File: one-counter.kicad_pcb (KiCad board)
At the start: 2 copper layers, 15 parts, among them J1 Conn_01x07-L, J2 Conn_01x07-R, U1 L7805, U2 555-L, U3 555-R, U4 74LS90-L, U5 74LS90-R, U6 7447-L, U7 7447-R, U8 5082-7650-L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

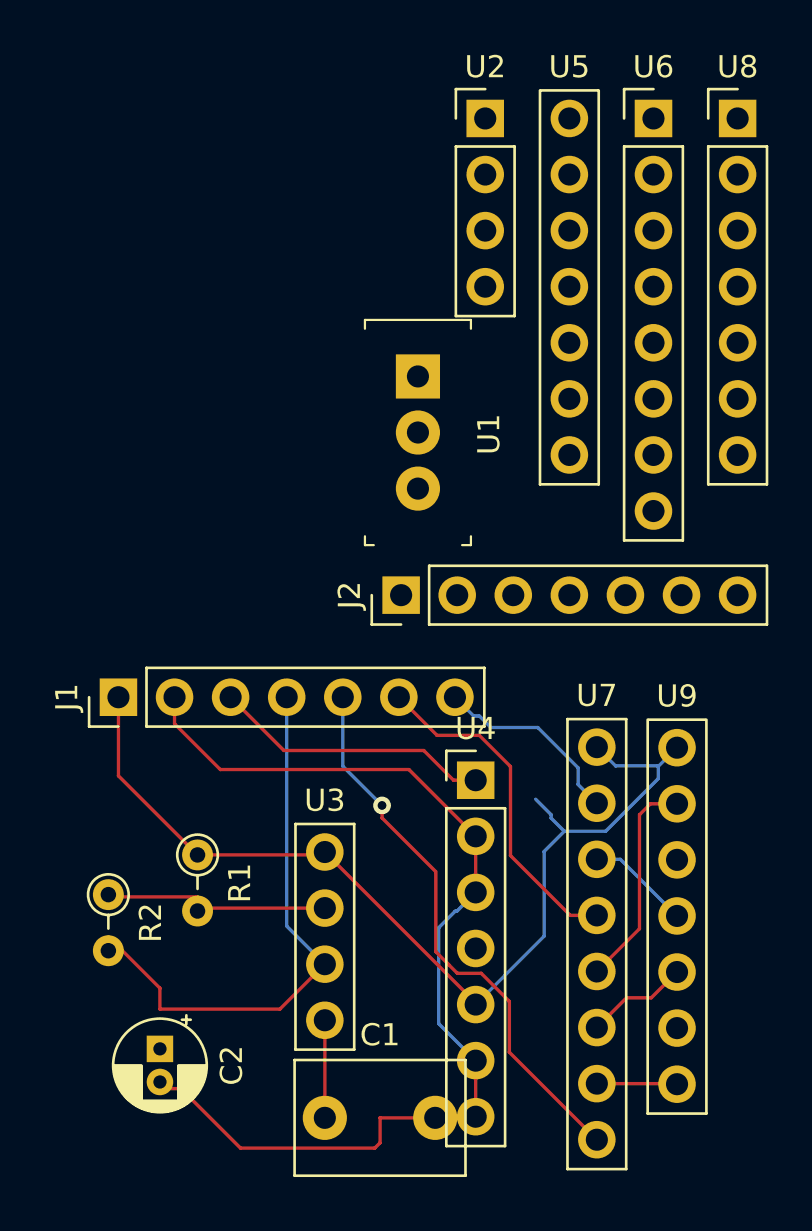
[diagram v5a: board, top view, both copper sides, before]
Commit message: bottom footprints mostly in place
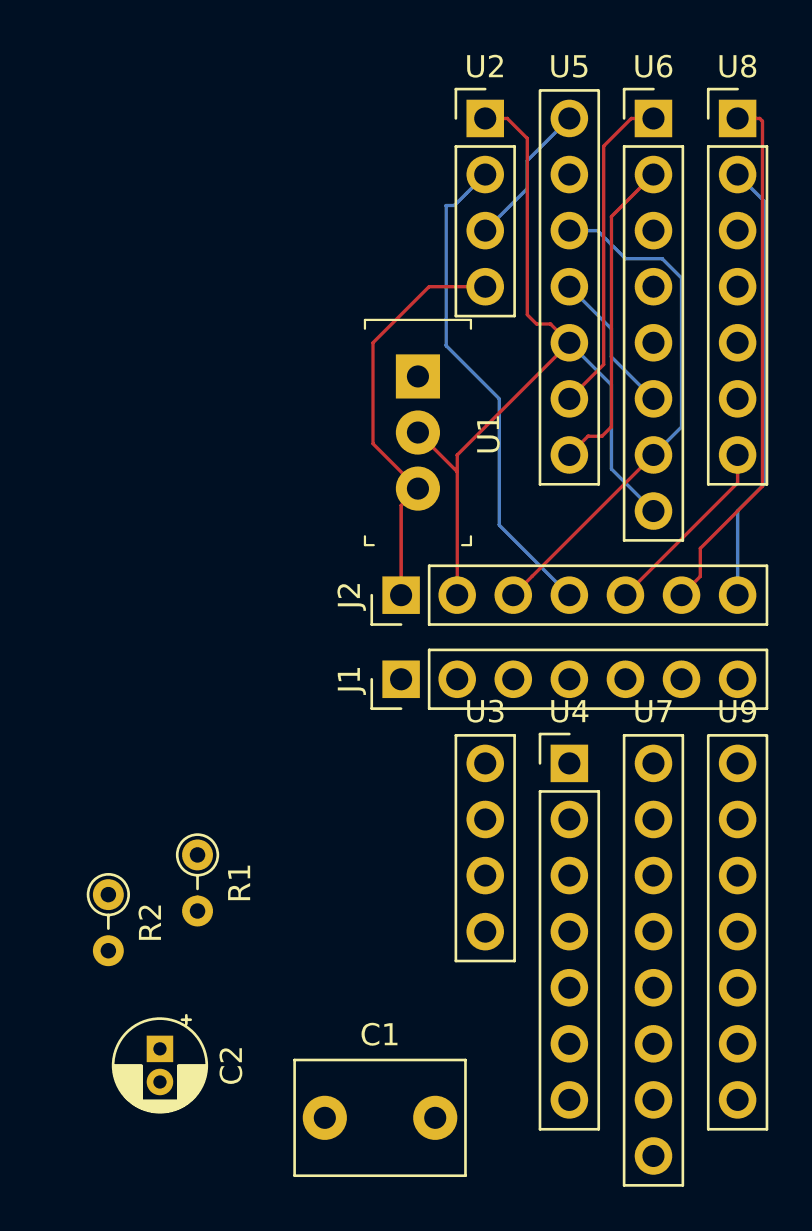
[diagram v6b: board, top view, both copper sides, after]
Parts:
- moved J1 12.8 mm to (162.6, 114.3)
- moved U3 8.30 mm to (166.4, 118.1)
- moved U4 4.31 mm to (170.2, 118.1)
- moved U9 2.83 mm to (177.8, 118.1)
- moved U7 2.67 mm to (174.0, 118.1)
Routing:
- net +5V: track 45.8 -> 18.7 mm
- net U7-9: track 25.5 -> 0.00 mm, vias 1 -> 0
- net U3-6: track 25.4 -> 0.00 mm
- net U8-1: track 0.00 -> 24.2 mm
- net U5-12: track 0.00 -> 23.5 mm
- net U2-2: track 0.00 -> 22.3 mm
- net U8-2: track 0.00 -> 20.1 mm
- net U7-13: track 15.4 -> 0.00 mm
- net Net-(U5-Pad9): track 0.00 -> 14.9 mm
- net Net-(U5-Pad8): track 0.00 -> 14.7 mm
- net U4-1: track 12.7 -> 0.00 mm
- net GND: track 47.8 -> 37.9 mm
- net Net-(U7-Pad12): track 9.80 -> 0.00 mm
- net Net-(R1-Pad2): track 10.1 -> 0.86 mm
- net U7-15: track 8.86 -> 0.00 mm
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
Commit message: move all components into place
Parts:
- C1: footprint Capacitor_THT:C_Disc_D7.5mm_W5.0mm_P5.00mm -> Capacitor_THT:C_Disc_D5.0mm_W2.5mm_P5.00mm
- moved R2 13.3 mm to (162.6, 123.2)
- moved C2 10.9 mm to (162.6, 131.4)
- moved R1 10.1 mm to (162.6, 118.1)
- moved C1 8.61 mm to (166.4, 129.5), turned to 270 degrees
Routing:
- net Net-(R1-Pad2): track 0.86 -> 0.00 mm
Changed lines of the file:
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@@
     (thickness 1.6)
     (drawings 0)
-    (tracks 63)
+    (tracks 61)
     (zones 0)
     (modules 15)
@@
     )
   )
-  (module Capacitor_THT:C_Disc_D7.5mm_W5.0mm_P5.00mm (layer F.Cu)
-    (at 159.1056 134.1628)
-    (descr "C, Disc series, Radial, pin pitch=5.00mm, , diameter*width=7.5*5.0mm^2, Capacitor, http://www.vishay.com/docs/28535/vy2series.pdf")
-    (tags "C Disc series Radial pin pitch 5.00mm  diameter 7.5mm width 5.0mm Capacitor")
-    (fp_text reference C1 (at 2.5 -3.75) (layer F.SilkS)
-      (effects (font (size 1 1) (thickness 0.15)))
-    )
-    (fp_text value 0.01uF (at 2.5 3.75) (layer F.Fab)
-      (effects (font (size 1 1) (thickness 0.15)))
-    )
-    (fp_line (start -1.25 -2.5) (end -1.25 2.5) (layer F.Fab) (width 0.1))
-    (fp_line (start -1.25 2.5) (end 6.25 2.5) (layer F.Fab) (width 0.1))
-    (fp_line (start 6.25 2.5) (end 6.25 -2.5) (layer F.Fab) (width 0.1))
-    (fp_line (start 6.25 -2.5) (end -1.25 -2.5) (layer F.Fab) (width 0.1))
-    (fp_line (start -1.37 -2.62) (end 6.37 -2.62) (layer F.SilkS) (width 0.12))
-    (fp_line (start -1.37 2.62) (end 6.37 2.62) (layer F.SilkS) (width 0.12))
-    (fp_line (start -1.37 -2.62) (end -1.37 2.62) (layer F.SilkS) (width 0.12))
-    (fp_line (start 6.37 -2.62) (end 6.37 2.62) (layer F.SilkS) (width 0.12))
-    (fp_line (start -1.5 -2.75) (end -1.5 2.75) (layer F.CrtYd) (width 0.05))
-    (fp_line (start -1.5 2.75) (end 6.5 2.75) (layer F.CrtYd) (width 0.05))
-    (fp_line (start 6.5 2.75) (end 6.5 -2.75) (layer F.CrtYd) (width 0.05))
-    (fp_line (start 6.5 -2.75) (end -1.5 -2.75) (layer F.CrtYd) (width 0.05))
-    (fp_text user %R (at 2.5 0) (layer F.Fab)
-      (effects (font (size 1 1) (thickness 0.15)))
-    )
-    (pad 1 thru_hole circle (at 0 0) (size 2 2) (drill 1) (layers *.Cu *.Mask)
-      (net 1 "Net-(C1-Pad1)"))
-    (pad 2 thru_hole circle (at 5 0) (size 2 2) (drill 1) (layers *.Cu *.Mask)
-      (net 2 GND))
-    (model ${KISYS3DMOD}/Capacitor_THT.3dshapes/C_Disc_D7.5mm_W5.0mm_P5.00mm.wrl
-      (at (xyz 0 0 0))
-      (scale (xyz 1 1 1))
-      (rotate (xyz 0 0 0))
-    )
-  )
   (module Capacitor_THT:CP_Radial_D4.0mm_P1.50mm (layer F.Cu)
-    (at 151.638 131.0386 270)
+    (at 162.56 131.445 270)
     (descr "CP, Radial series, Radial, pin pitch=1.50mm, , diameter=4mm, Electrolytic Capacitor")
     (tags "CP Radial series Radial pin pitch 1.50mm  diameter 4mm Electrolytic Capacitor")
@@
   )
   (module Resistor_THT:R_Axial_DIN0204_L3.6mm_D1.6mm_P2.54mm_Vertical (layer F.Cu)
-    (at 153.3398 122.2552 270)
+    (at 162.56 118.11 270)
     (descr "Resistor, Axial_DIN0204 series, Axial, Vertical, pin pitch=2.54mm, 0.167W, length*diameter=3.6*1.6mm^2, http://cdn-reichelt.de/documents/datenblatt/B400/1_4W%23YAG.pdf")
     (tags "Resistor Axial_DIN0204 series Axial Vertical pin pitch 2.54mm 0.167W length 3.6mm diameter 1.6mm")
@@
   )
   (module Resistor_THT:R_Axial_DIN0204_L3.6mm_D1.6mm_P2.54mm_Vertical (layer F.Cu)
-    (at 149.3012 124.0536 270)
+    (at 162.56 123.19 270)
     (descr "Resistor, Axial_DIN0204 series, Axial, Vertical, pin pitch=2.54mm, 0.167W, length*diameter=3.6*1.6mm^2, http://cdn-reichelt.de/documents/datenblatt/B400/1_4W%23YAG.pdf")
     (tags "Resistor Axial_DIN0204 series Axial Vertical pin pitch 2.54mm 0.167W length 3.6mm diameter 1.6mm")
@@
       (net 4 "Net-(R1-Pad2)"))
     (model ${KISYS3DMOD}/Resistor_THT.3dshapes/R_Axial_DIN0204_L3.6mm_D1.6mm_P2.54mm_Vertical.wrl
+      (at (xyz 0 0 0))
+      (scale (xyz 1 1 1))
+      (rotate (xyz 0 0 0))
+    )
+  )
+  (module Capacitor_THT:C_Disc_D5.0mm_W2.5mm_P5.00mm (layer F.Cu)
+    (at 166.37 129.54 270)
+    (descr "C, Disc series, Radial, pin pitch=5.00mm, , diameter*width=5*2.5mm^2, Capacitor, http://cdn-reichelt.de/documents/datenblatt/B300/DS_KERKO_TC.pdf")
+    (tags "C Disc series Radial pin pitch 5.00mm  diameter 5mm width 2.5mm Capacitor")
+    (fp_text reference C1 (at 2.5 -2.5 270) (layer F.SilkS)
+      (effects (font (size 1 1) (thickness 0.15)))
+    )
+    (fp_text value 0.01uF (at 2.5 2.5 270) (layer F.Fab)
+      (effects (font (size 1 1) (thickness 0.15)))
+    )
+    (fp_line (start 0 -1.25) (end 0 1.25) (layer F.Fab) (width 0.1))
+    (fp_line (start 0 1.25) (end 5 1.25) (layer F.Fab) (width 0.1))
+    (fp_line (start 5 1.25) (end 5 -1.25) (layer F.Fab) (width 0.1))
+    (fp_line (start 5 -1.25) (end 0 -1.25) (layer F.Fab) (width 0.1))
+    (fp_line (start -0.12 -1.37) (end 5.12 -1.37) (layer F.SilkS) (width 0.12))
+    (fp_line (start -0.12 1.37) (end 5.12 1.37) (layer F.SilkS) (width 0.12))
+    (fp_line (start -0.12 -1.37) (end -0.12 -1.055) (layer F.SilkS) (width 0.12))
+    (fp_line (start -0.12 1.055) (end -0.12 1.37) (layer F.SilkS) (width 0.12))
+    (fp_line (start 5.12 -1.37) (end 5.12 -1.055) (layer F.SilkS) (width 0.12))
+    (fp_line (start 5.12 1.055) (end 5.12 1.37) (layer F.SilkS) (width 0.12))
+    (fp_line (start -1.05 -1.5) (end -1.05 1.5) (layer F.CrtYd) (width 0.05))
+    (fp_line (start -1.05 1.5) (end 6.05 1.5) (layer F.CrtYd) (width 0.05))
+    (fp_line (start 6.05 1.5) (end 6.05 -1.5) (layer F.CrtYd) (width 0.05))
+    (fp_line (start 6.05 -1.5) (end -1.05 -1.5) (layer F.CrtYd) (width 0.05))
+    (fp_text user %R (at 2.5 0 270) (layer F.Fab)
+      (effects (font (size 1 1) (thickness 0.15)))
+    )
+    (pad 1 thru_hole circle (at 0 0 270) (size 1.6 1.6) (drill 0.8) (layers *.Cu *.Mask)
+      (net 1 "Net-(C1-Pad1)"))
+    (pad 2 thru_hole circle (at 5 0 270) (size 1.6 1.6) (drill 0.8) (layers *.Cu *.Mask)
+      (net 2 GND))
+    (model ${KISYS3DMOD}/Capacitor_THT.3dshapes/C_Disc_D5.0mm_W2.5mm_P5.00mm.wrl
       (at (xyz 0 0 0))
       (scale (xyz 1 1 1))
@@
   (segment (start 163.322 105.664) (end 161.29 103.632) (width 0.1524) (layer F.Cu) (net 3))
   (segment (start 166.37 96.52) (end 163.83 96.52) (width 0.1524) (layer F.Cu) (net 3))
-  (segment (start 153.8478 124.6632) (end 153.3398 124.1552) (width 0.1524) (layer F.Cu) (net 4))
-  (segment (start 149.4028 124.1552) (end 149.3012 124.0536) (width 0.1524) (layer F.Cu) (net 4))
   (segment (start 168.275 90.805) (end 170.18 88.9) (width 0.1524) (layer B.Cu) (net 5))
   (segment (start 166.37 93.98) (end 168.275 92.075) (width 0.1524) (layer B.Cu) (net 5))

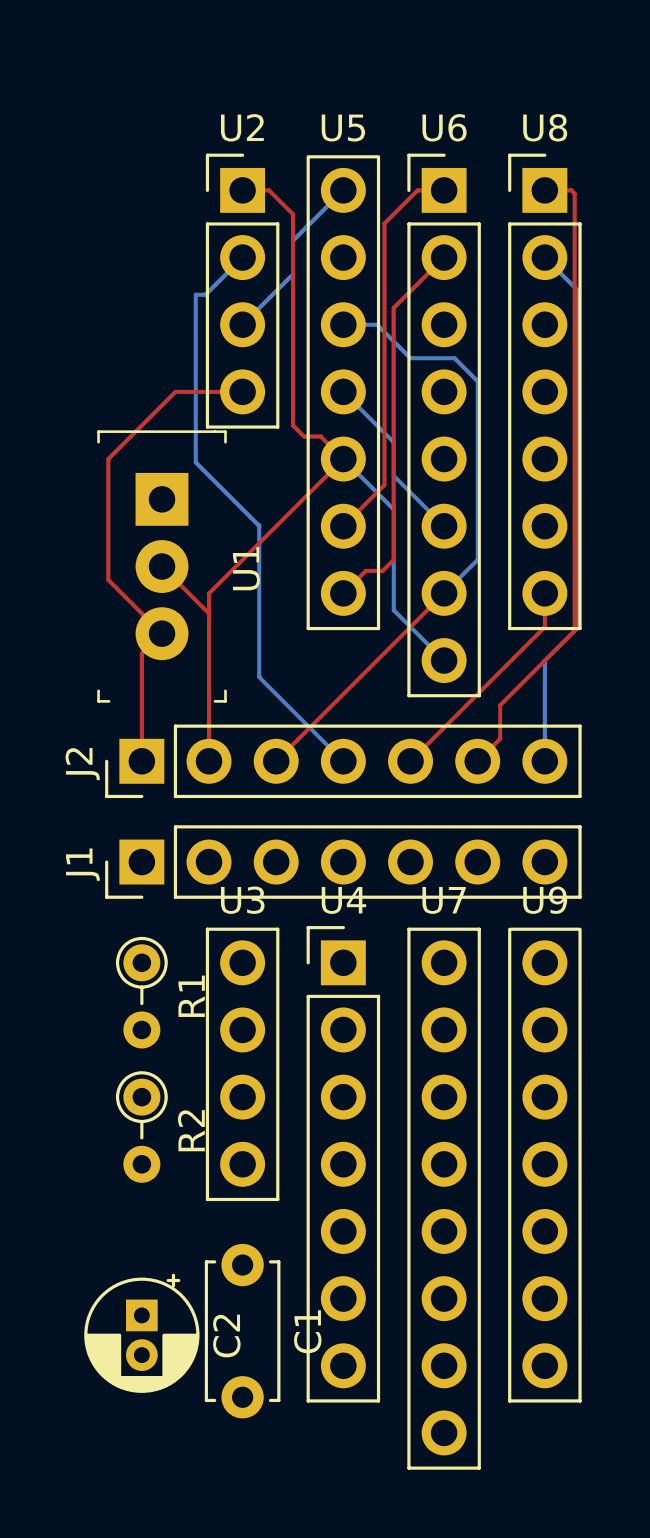
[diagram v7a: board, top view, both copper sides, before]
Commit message: flip connector on top  half
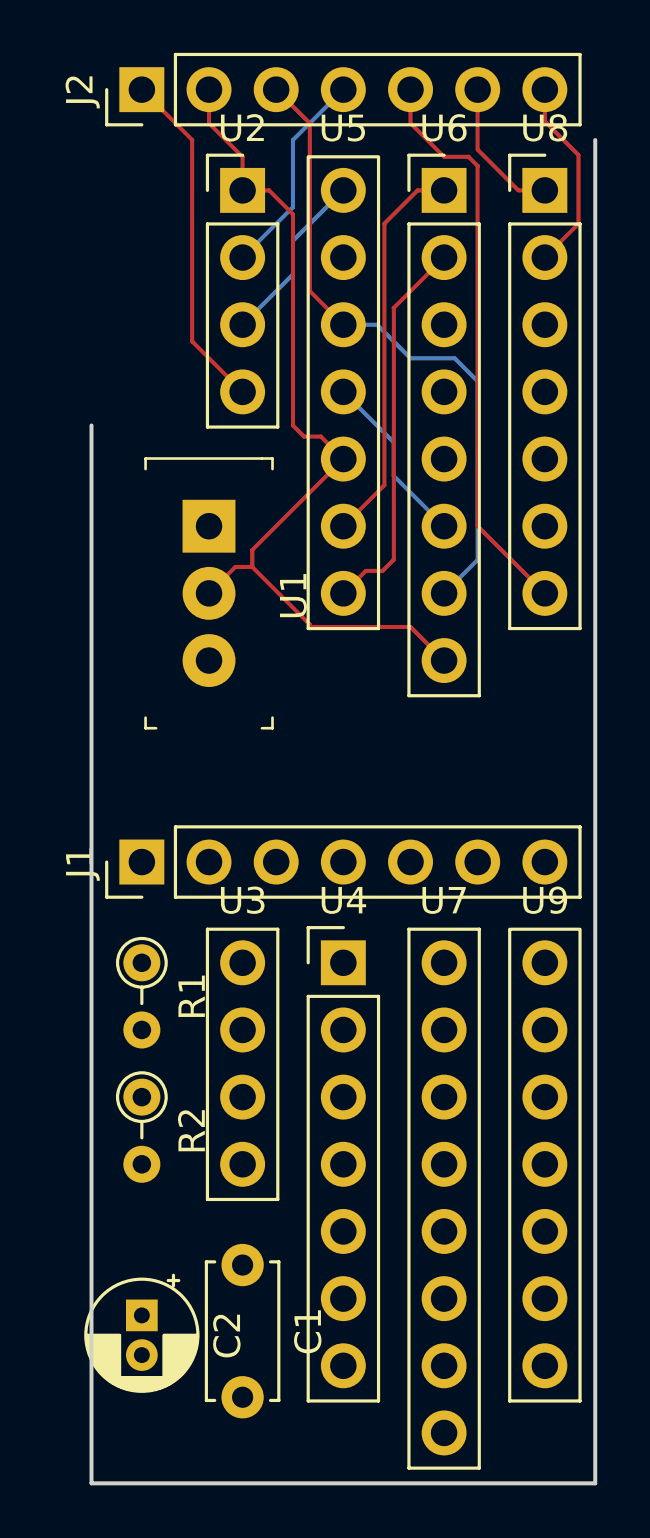
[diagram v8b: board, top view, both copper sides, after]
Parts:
- moved J2 25.4 mm to (162.6, 85.1)
- moved U1 2.05 mm to (165.1, 101.6)
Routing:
- net U8-1: track 24.2 -> 5.45 mm
- net U2-2: track 22.3 -> 7.93 mm
- net U8-7: track 8.45 -> 21.7 mm
- net U8-2: track 20.1 -> 7.40 mm
- net +5V: track 18.7 -> 13.0 mm
- net GND: track 37.9 -> 33.4 mm
- net U5-12: track 23.5 -> 24.5 mm
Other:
- board outline added: 19.1 x 50.8 mm
